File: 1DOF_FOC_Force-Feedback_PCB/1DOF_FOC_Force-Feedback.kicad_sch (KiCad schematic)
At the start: 5 parts, among them U4 AS5047P ADAPTERBOARD, U6 GBM2804

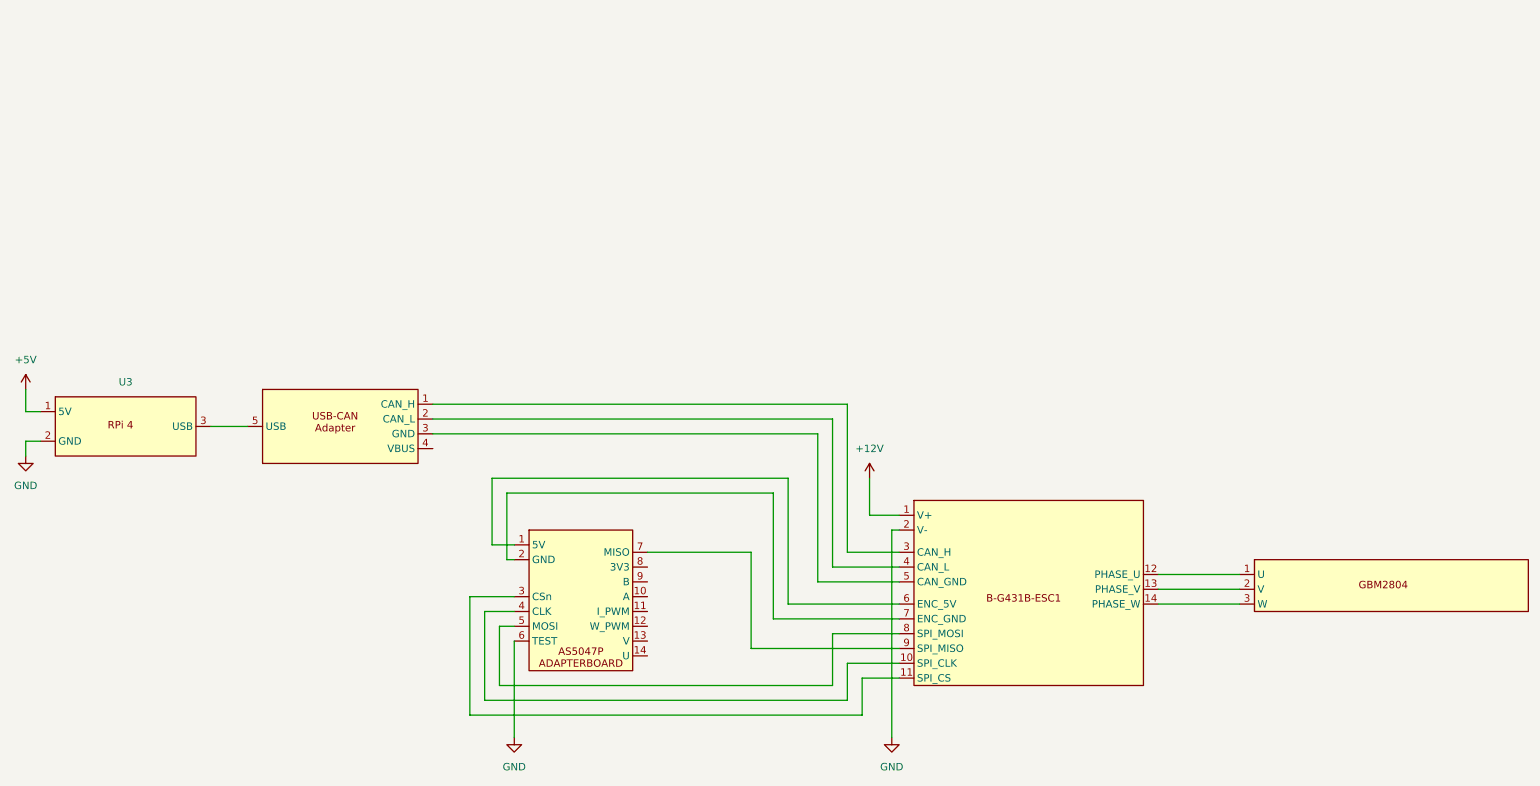
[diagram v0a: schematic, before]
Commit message: Added second motor and BOM
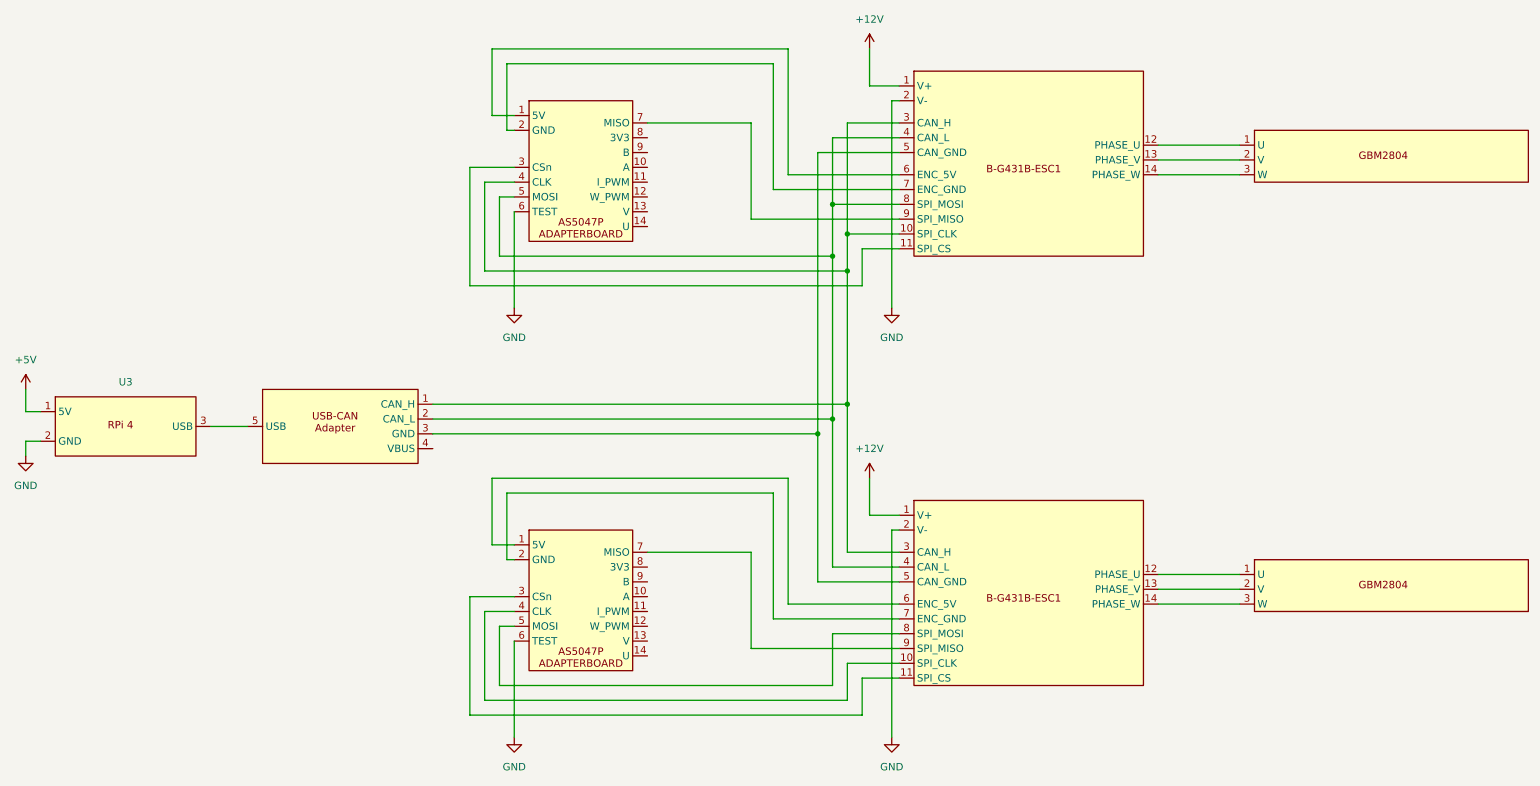
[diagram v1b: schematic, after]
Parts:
- added U5: AS5047P ADAPTERBOARD, symbol my_components:AS5047P
- added U7: (no value), symbol my_components:STM32G431BESC
- added U8: GBM2804, symbol my_components:GBM2804
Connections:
- net +12V: now also U7.1 (V+)
- net GND: now also U5.6 (TEST), U7.2 (V-)
- net at U1.1 (CAN_H), U2.3 (CAN_H): now also U5.4 (CLK), U7.10 (SPI_CLK), U7.3 (CAN_H)
- net at U1.2 (CAN_L), U2.4 (CAN_L): now also U5.5 (MOSI), U7.4 (CAN_L), U7.8 (SPI_MOSI)
- net at U1.3 (GND), U2.5 (CAN_GND): now also U7.5 (CAN_GND)
- new net: U5.1 (5V), U7.6 (ENC_5V)
- new net: U5.2 (GND), U7.7 (ENC_GND)
- new net: U5.3 (CSn), U7.11 (SPI_CS)
- new net: U5.7 (MISO), U7.9 (SPI_MISO)
- new net: U7.12 (PHASE_U), U8.1 (U)
- new net: U7.13 (PHASE_V), U8.2 (V)
- new net: U7.14 (PHASE_W), U8.3 (W)
